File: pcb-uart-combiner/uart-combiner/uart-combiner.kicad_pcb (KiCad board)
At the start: 2 copper layers, 52.2 x 82.2 mm, 26 parts, among them J1 Conn_01x03, J5 DBG UART, J6 SWD, J7 Conn_01x03, J8 Conn_01x03, J9 Conn_01x03

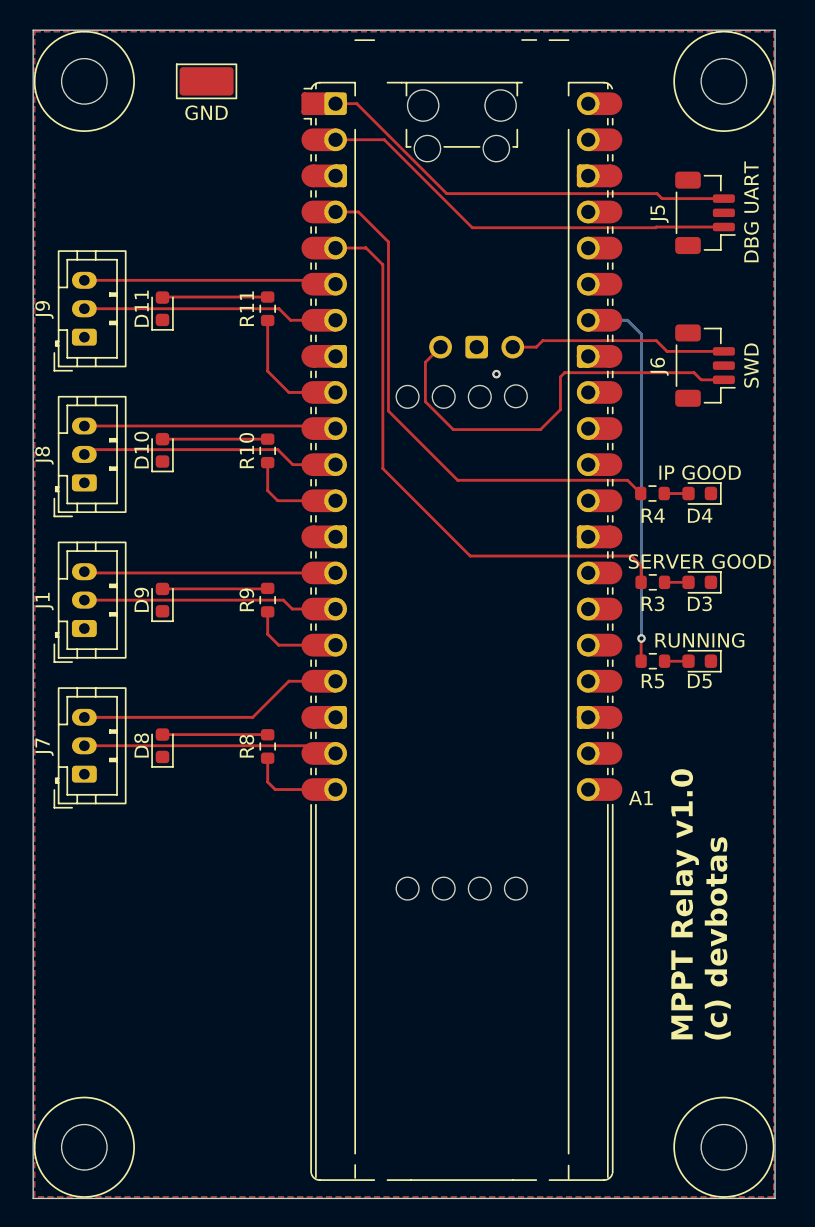
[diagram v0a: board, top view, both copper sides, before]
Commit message: Adjusting board size.
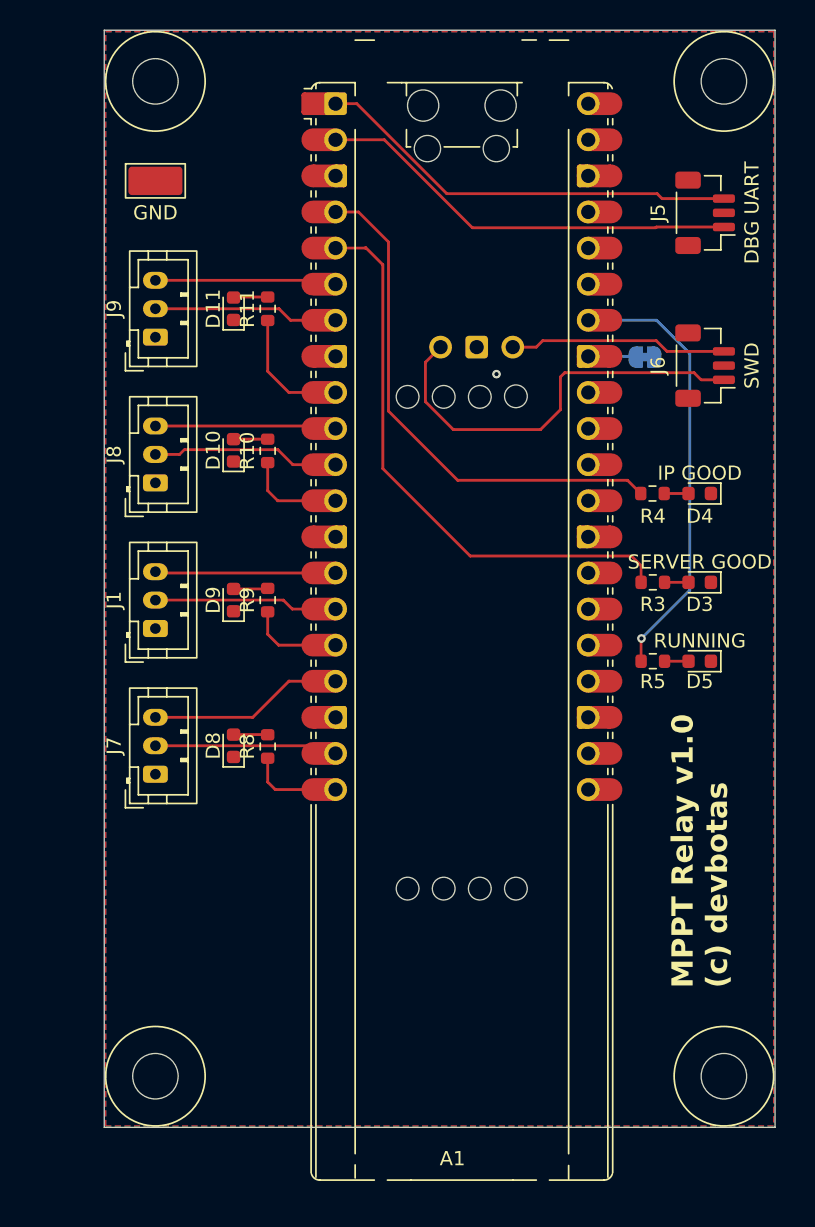
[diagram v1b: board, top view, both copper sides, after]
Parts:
- added JP1: Jumper_2_Bridged, Jumper:SolderJumper-2_P1.3mm_Bridged_RoundedPad1.0x1.5mm, B.Cu at (149.4, 94.4)
- A1: value RaspberryPi_Pico -> WizNet W55RP20 EVB Pico
- moved TP1 7.87 mm to (115.0, 82.0)
- moved H3 7.07 mm to (115.0, 145.0)
- moved D10 5.00 mm to (120.5, 101.0)
- moved D11 5.00 mm to (120.5, 91.0)
- moved D8 5.00 mm to (120.5, 121.8)
- moved D9 5.00 mm to (120.5, 111.5)
- moved H1 5.00 mm to (115.0, 75.0)
- moved H4 5.00 mm to (155.0, 145.0)
- moved J1 5.00 mm to (115.0, 113.5)
- moved J7 5.00 mm to (115.0, 123.8)
- moved J8 5.00 mm to (115.0, 103.2)
- moved J9 5.00 mm to (115.0, 93.0)
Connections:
- A1 pad 33: unconnected-(A1-AGND-Pad33) -> Net-(A1-AGND)
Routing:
- net Net-(D10-A): track 7.40 -> 2.35 mm
- net Net-(A1-GPIO7): track 17.7 -> 12.7 mm
- net Net-(D9-A): track 7.42 -> 2.42 mm
- net Net-(D8-A): track 7.41 -> 2.41 mm
- net Net-(D11-A): track 7.42 -> 2.42 mm
- net Net-(A1-GPIO5): track 18.0 -> 13.0 mm
- net Net-(A1-GPIO4): track 17.8 -> 12.8 mm
- net Net-(A1-GPIO13): track 18.7 -> 13.7 mm
- net Net-(A1-GPIO10): track 17.7 -> 12.7 mm
- net Net-(A1-GPIO14): track 17.9 -> 12.9 mm
- net Net-(A1-GPIO11): track 17.9 -> 12.9 mm
- net Net-(A1-GPIO8): track 17.5 -> 12.9 mm
- net Net-(A1-GPIO28_ADC2): track 27.2 -> 31.2 mm
- net Net-(A1-AGND): track 0.00 -> 3.37 mm
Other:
- board size 52.2 x 82.2 mm -> 47.2 x 77.2 mm

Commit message: Tuning UART combiner.
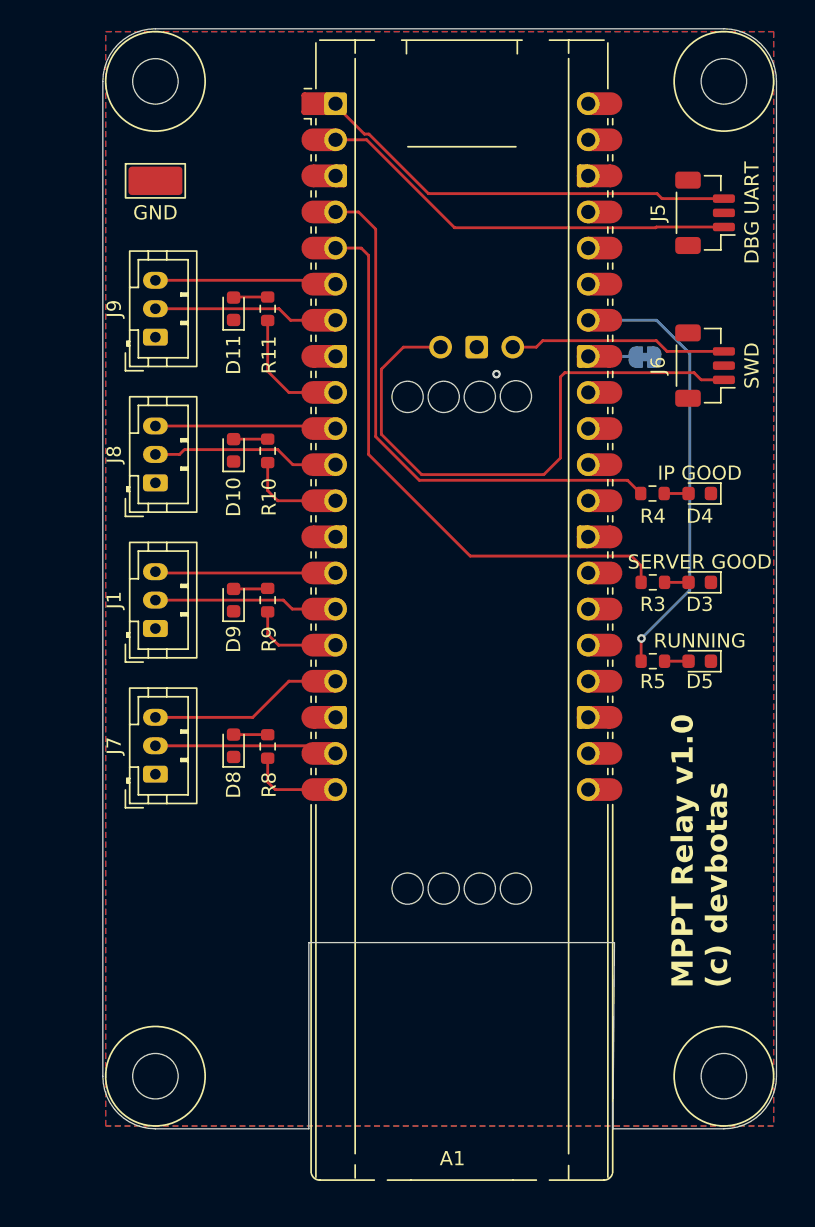
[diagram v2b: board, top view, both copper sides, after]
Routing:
- net Net-(A1-SWCLK): track 29.3 -> 41.2 mm
- net Net-(A1-GPIO2): track 36.7 -> 38.2 mm
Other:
- board size 47.2 x 77.2 mm -> 47.4 x 77.4 mm

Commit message: Fine tuning UART combiner.
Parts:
- J1: renamed from J9; value Conn_01x03 -> UART1/I2C0; footprint Connector_JST:JST_PH_B3B-PH-K_1x03_P2.00mm_Vertical -> Connector_JST:JST_PH_B4B-PH-K_1x04_P2.00mm_Vertical
- J2: renamed from J1; value Conn_01x03 -> I2C1; footprint Connector_JST:JST_PH_B3B-PH-K_1x03_P2.00mm_Vertical -> Connector_JST:JST_PH_B4B-PH-K_1x04_P2.00mm_Vertical
- J3: renamed from J8; footprint Connector_JST:JST_PH_B3B-PH-K_1x03_P2.00mm_Vertical -> Connector_JST:JST_PH_B4B-PH-K_1x04_P2.00mm_Vertical
- J4: renamed from J7; footprint Connector_JST:JST_PH_B3B-PH-K_1x03_P2.00mm_Vertical -> Connector_JST:JST_PH_B4B-PH-K_1x04_P2.00mm_Vertical
- moved J4 3.75 mm to (115.0, 127.5)
- moved D6 2.75 mm to (120.5, 124.5)
- moved R6 2.75 mm to (122.9, 124.5)
- moved J2 2.50 mm to (115.0, 116.0)
- moved D5 1.50 mm to (120.5, 113.0)
- moved R5 1.50 mm to (122.9, 113.0)
- moved J3 1.25 mm to (115.0, 104.5)
- moved D4 0.54 mm to (120.5, 101.5)
- moved R4 0.54 mm to (122.9, 101.5)
- moved TP1 0.50 mm to (115.0, 81.5), turned to 90 degrees
- renumbered D4 to D1, D3 to D2, D11 to D3, D10 to D4, D9 to D5, D8 to D6, D5 to D7, R4 to R1, R3 to R2, R11 to R3, R10 to R4, R9 to R5, R8 to R6, R5 to R7
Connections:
- A1 pad 36: unconnected-(A1-3V3-Pad36)_1 -> +3V3
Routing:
- net +3V3: track 0.00 -> 74.5 mm
- net Net-(A1-GPIO15): track 6.67 -> 5.10 mm
- net Net-(A1-GPIO13): track 13.7 -> 15.3 mm
- net Net-(A1-GPIO12): track 6.67 -> 5.13 mm
- net Net-(A1-GPIO28_ADC2): track 31.2 -> 32.3 mm
- net Net-(A1-GPIO10): track 12.7 -> 13.7 mm
- net Net-(A1-GPIO8): track 12.9 -> 13.7 mm
- net Net-(A1-GPIO7): track 12.7 -> 13.3 mm
- net Net-(A1-GPIO9): track 7.04 -> 6.51 mm
- net Net-(A1-GPIO11): track 12.9 -> 13.4 mm
- net GND: vias 1 -> 13
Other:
- board text added: "UART combiner v1.0 (c) devbotas"
- board text removed: "MPPT Relay v1.0 (c) devbotas"
